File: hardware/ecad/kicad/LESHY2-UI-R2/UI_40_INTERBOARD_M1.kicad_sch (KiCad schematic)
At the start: 1 part, among them J18 Hirose FX8C-80P-SV1(92)

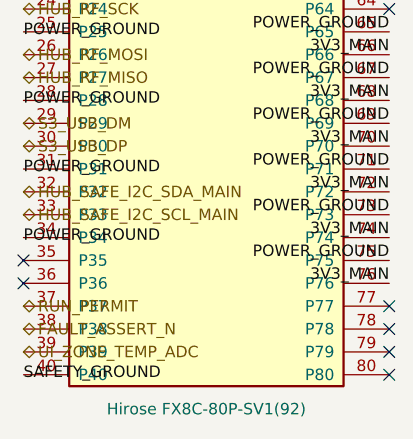
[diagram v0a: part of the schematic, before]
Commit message: Review R2 startup and fault-display sequencing
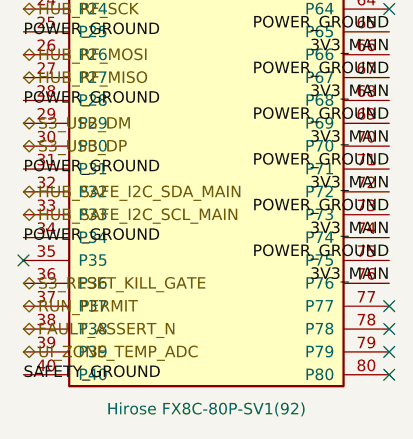
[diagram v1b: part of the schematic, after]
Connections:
- net S3_RESET_KILL_GATE: now reaches J18.36 (P36)
- no-connect marks 11 -> 10
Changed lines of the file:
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@@
 	(no_connect (at 35.56 134.62)
 	)
-	(no_connect (at 35.56 137.16)
+	(hierarchical_label "S3_RESET_KILL_GATE"
+		(shape bidirectional)
+		(at 35.56 137.16 0)
+		(effects (font (size 1.27 1.27)))
 	)
 	(hierarchical_label "RUN_PERMIT"

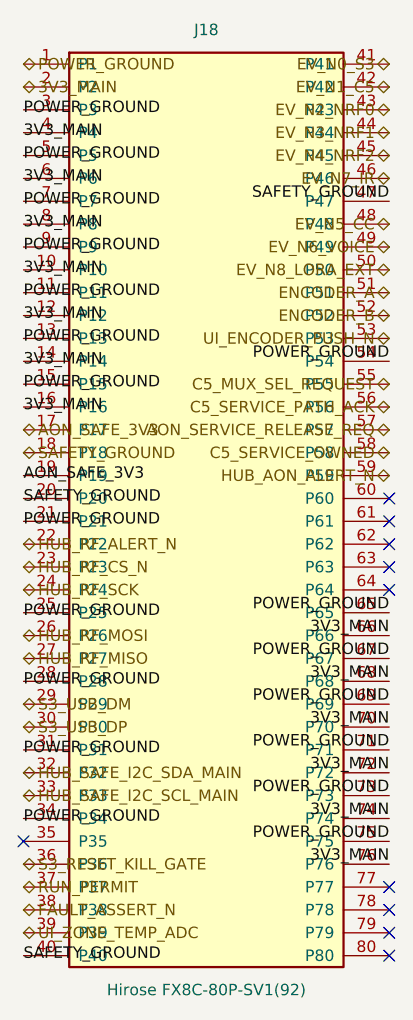
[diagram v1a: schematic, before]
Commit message: Review R2 power transitions and watchdog
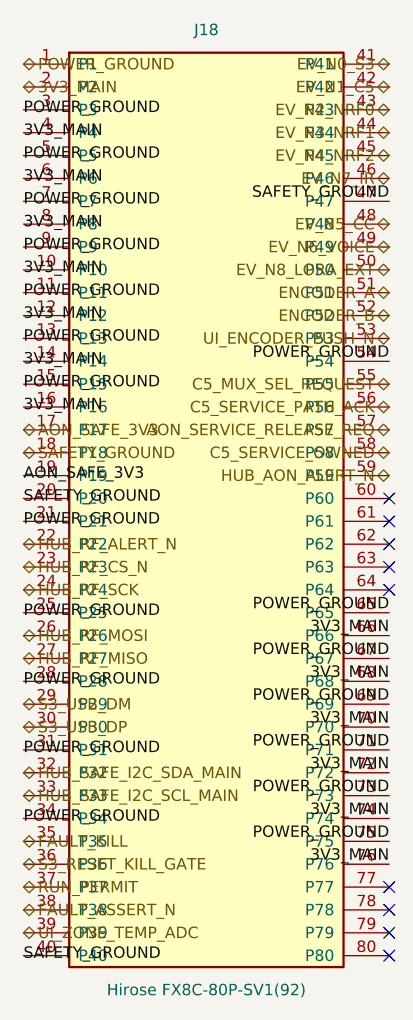
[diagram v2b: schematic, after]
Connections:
- net FAULT_KILL: now reaches J18.35 (P35)
- no-connect marks 10 -> 9
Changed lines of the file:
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@@
 		(effects (font (size 1.27 1.27)))
 	)
-	(no_connect (at 35.56 134.62)
+	(hierarchical_label "FAULT_KILL"
+		(shape bidirectional)
+		(at 35.56 134.62 0)
+		(effects (font (size 1.27 1.27)))
 	)
 	(hierarchical_label "S3_RESET_KILL_GATE"

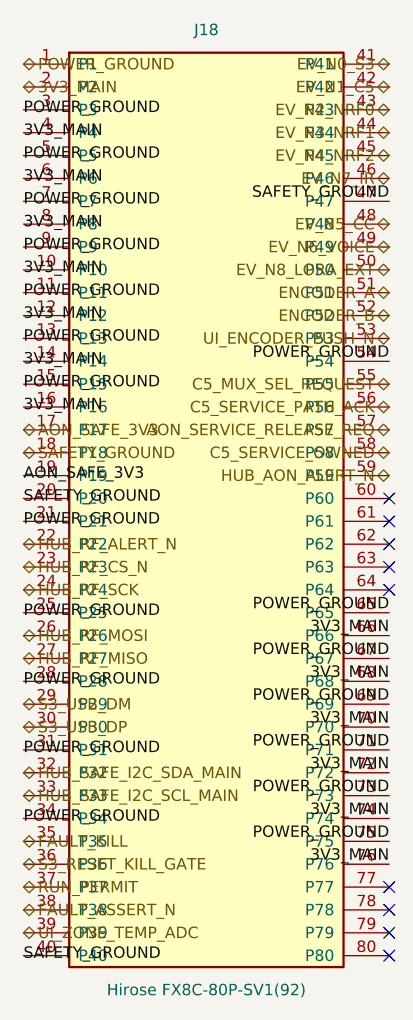
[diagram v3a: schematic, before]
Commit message: Bind H6 RF and USB routing geometry
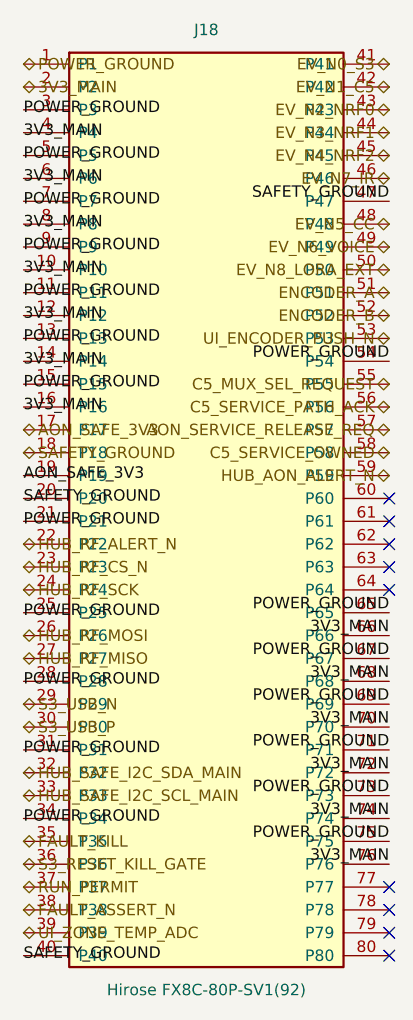
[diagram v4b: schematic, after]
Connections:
- net S3_USB_DM renamed S3_USB_N
- net S3_USB_DP renamed S3_USB_P
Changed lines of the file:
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@@
 		(effects (font (size 1.27 1.27)))
 	)
-	(hierarchical_label "S3_USB_DM"
+	(hierarchical_label "S3_USB_N"
 		(shape bidirectional)
 		(at 35.56 119.38 0)
 		(effects (font (size 1.27 1.27)))
 	)
-	(hierarchical_label "S3_USB_DP"
+	(hierarchical_label "S3_USB_P"
 		(shape bidirectional)
 		(at 35.56 121.92 0)

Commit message: Canonicalize physical ground anchors
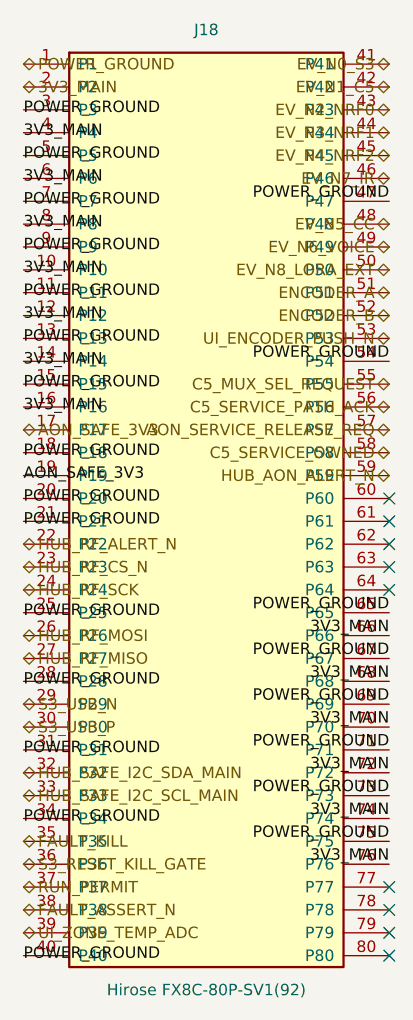
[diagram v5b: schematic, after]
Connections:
- net SAFETY_GROUND is gone; now on net POWER_GROUND: J18.18 (P18), J18.20 (P20), J18.40 (P40), J18.47 (P47)
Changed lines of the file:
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@@
 		(effects (font (size 1.27 1.27)))
 	)
-	(hierarchical_label "SAFETY_GROUND"
-		(shape bidirectional)
+	(label "POWER_GROUND"
 		(at 35.56 91.44 0)
 		(effects (font (size 1.27 1.27)))
@@
 		(effects (font (size 1.27 1.27)))
 	)
-	(label "SAFETY_GROUND"
+	(label "POWER_GROUND"
 		(at 35.56 96.52 0)
 		(effects (font (size 1.27 1.27)))
@@
 		(effects (font (size 1.27 1.27)))
 	)
-	(label "SAFETY_GROUND"
+	(label "POWER_GROUND"
 		(at 35.56 147.32 0)
 		(effects (font (size 1.27 1.27)))
@@
 		(effects (font (size 1.27 1.27)) (justify right bottom))
 	)
-	(label "SAFETY_GROUND"
+	(label "POWER_GROUND"
 		(at 76.20 63.50 180)
 		(effects (font (size 1.27 1.27)) (justify right bottom))
